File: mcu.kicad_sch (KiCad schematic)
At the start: 11 parts

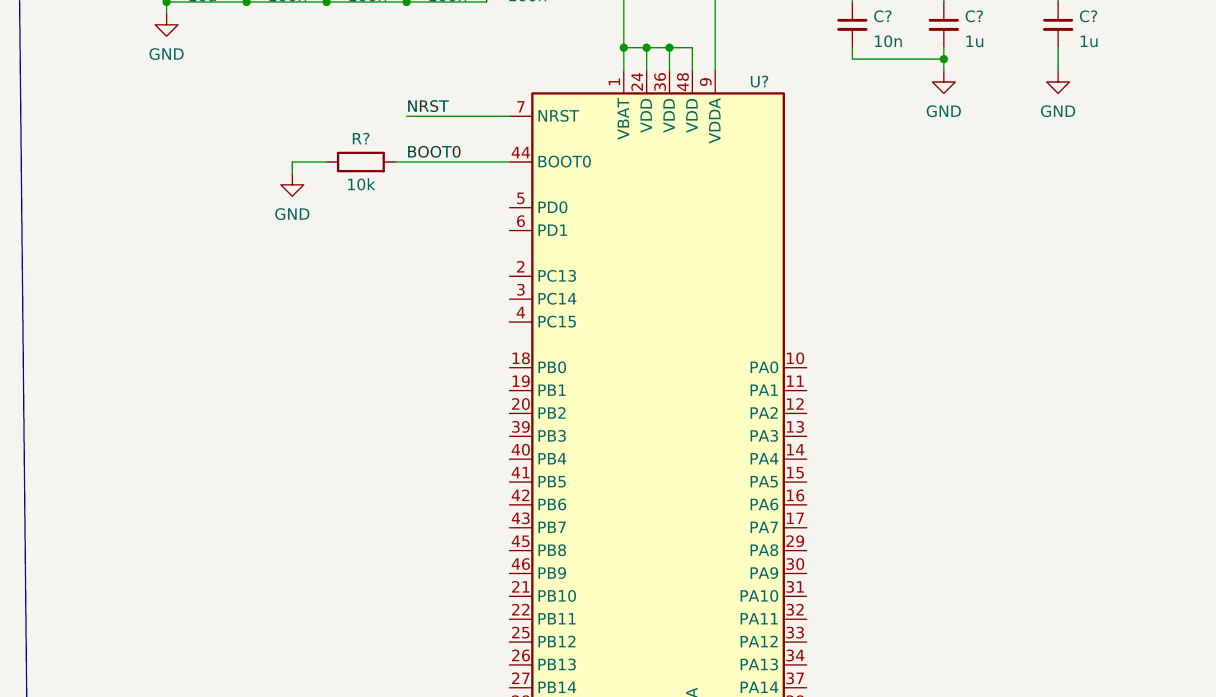
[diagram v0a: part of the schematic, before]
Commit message: Added crystal oscillator.
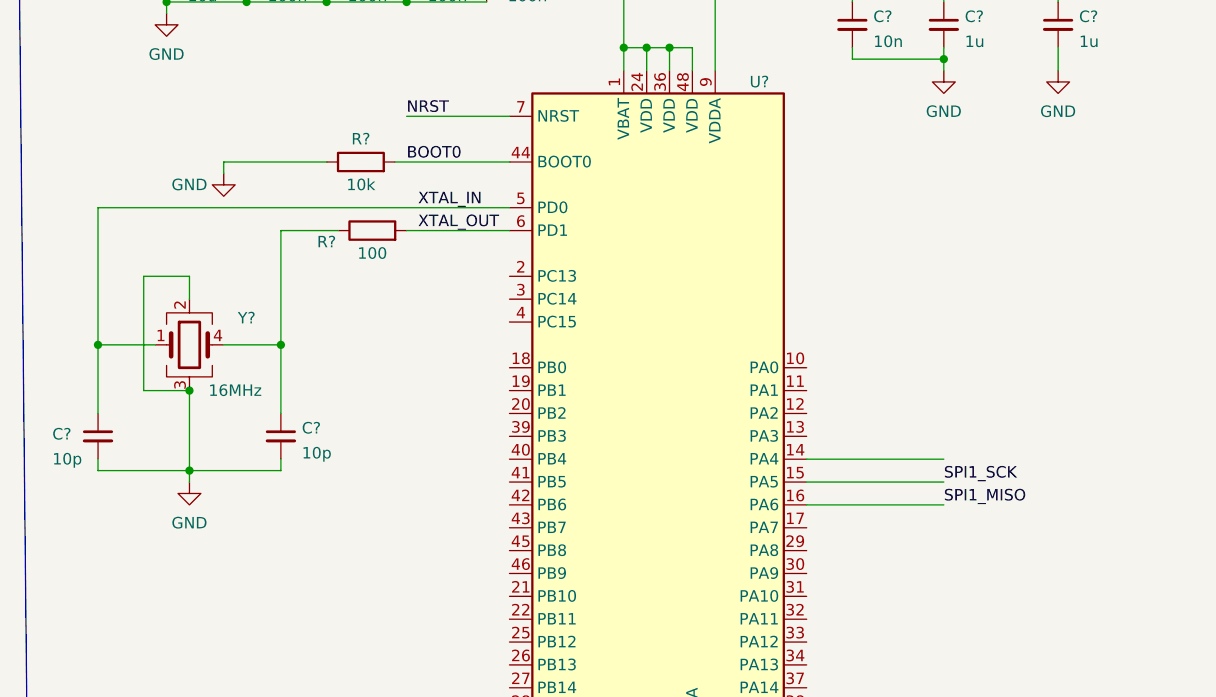
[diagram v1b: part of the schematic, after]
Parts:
- added C? (x2): 10p, symbol Device:C_Small
- added R?: 100, symbol Device:R
- added Y?: 16MHz, symbol Device:Crystal_GND23
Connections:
- net GND: now also C?.2, C?.2, Y?.2, Y?.3
- net SPI1_SCK: now reaches U?.15 (PA5)
- net SPI1_MISO: now reaches U?.16 (PA6)
- net XTAL_IN: now reaches U?.5 (PD0)
- net XTAL_IN: now also C?.1, Y?.1
- net XTAL_OUT: now reaches U?.6 (PD1)
- net XTAL_OUT: now also R?.2
- new net: C?.1, R?.1, Y?.4

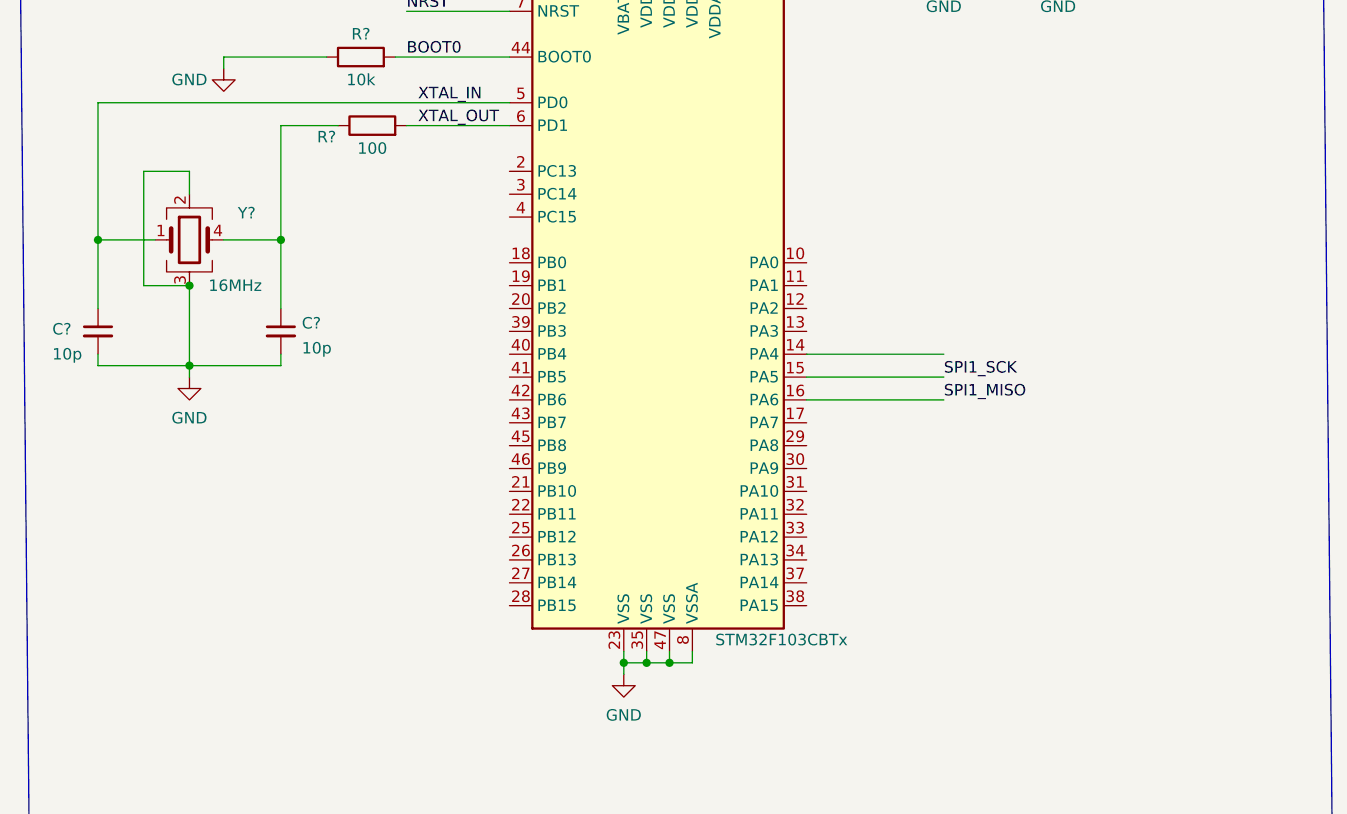
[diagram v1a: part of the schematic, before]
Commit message: Completed MCU circuitry
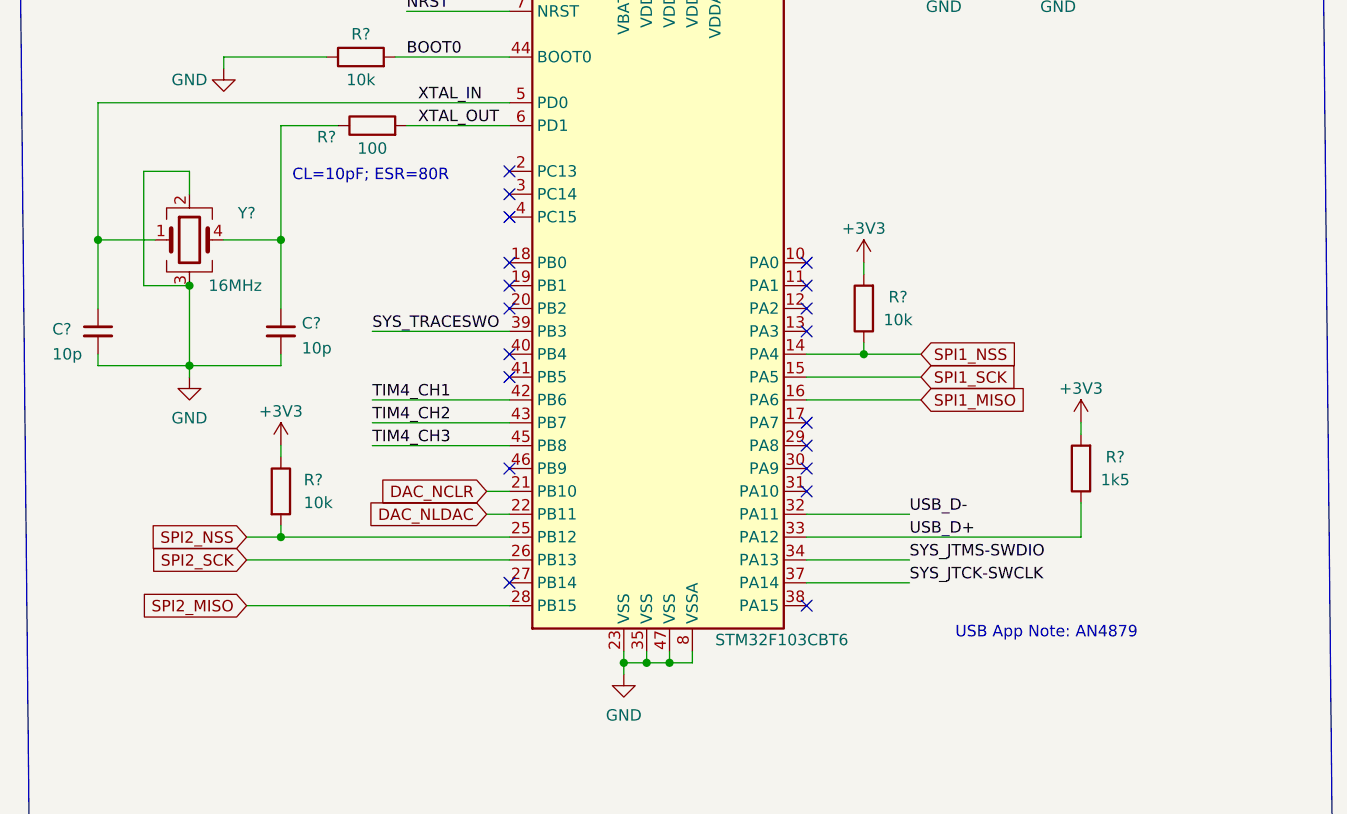
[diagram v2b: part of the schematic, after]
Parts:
- added R?: 1k5, symbol Device:R
- added R? (x2): 10k, symbol Device:R
- U?: value STM32F103CBTx -> STM32F103CBT6
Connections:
- net +3V3: now also R?.1, R?.2, R?.2
- net SPI1_NSS: now reaches U?.14 (PA4)
- net SPI1_NSS: now also R?.1
- net DAC_NCLR: now reaches U?.21 (PB10)
- net DAC_NLDAC: now reaches U?.22 (PB11)
- net SPI2_NSS: now reaches U?.25 (PB12)
- net SPI2_NSS: now also R?.2
- net SPI2_SCK: now reaches U?.26 (PB13)
- net SPI2_MISO: now reaches U?.28 (PB15)
- net USB_D-: now reaches U?.32 (PA11)
- net USB_D+: now reaches U?.33 (PA12)
- net USB_D+: now also R?.1
- net SYS_JTMS-SWDIO: now reaches U?.34 (PA13)
- net SYS_JTCK-SWCLK: now reaches U?.37 (PA14)
- net SYS_TRACESWO: now reaches U?.39 (PB3)
- net TIM4_CH1: now reaches U?.42 (PB6)
- net TIM4_CH2: now reaches U?.43 (PB7)
- net TIM4_CH3: now reaches U?.45 (PB8)
- no-connect marks 0 -> 19
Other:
- note added: "CL=10pF; ESR=80R"
- note added: "USB App Note: AN4879"

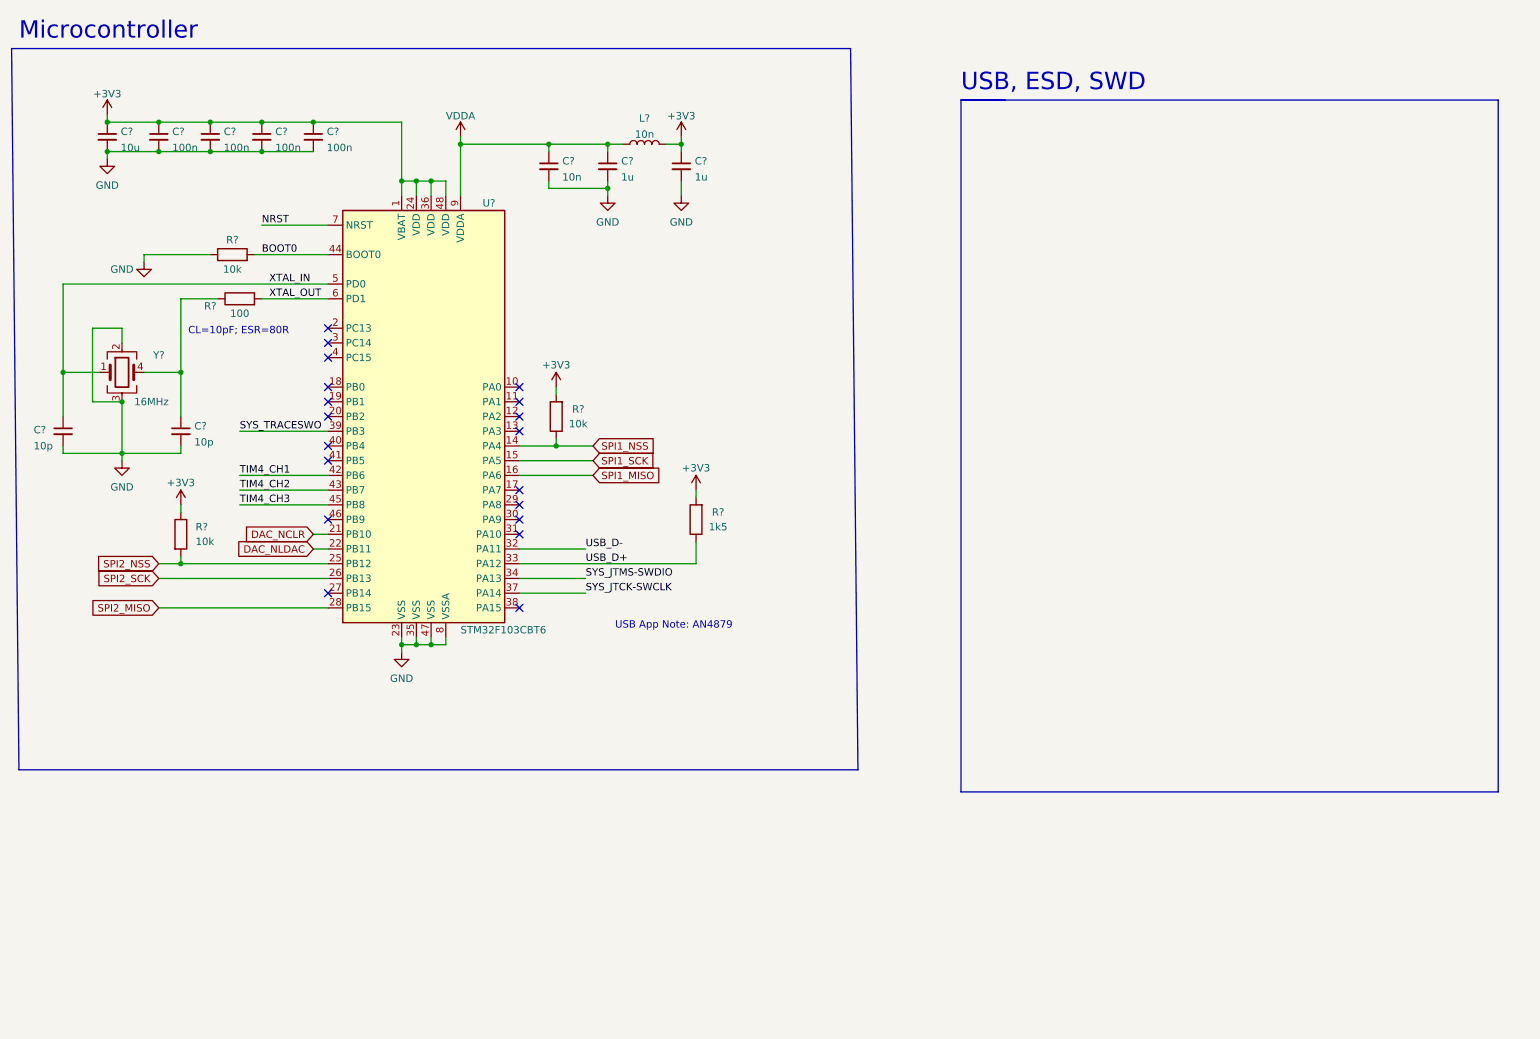
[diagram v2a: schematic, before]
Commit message: Completed USB Type C connection.
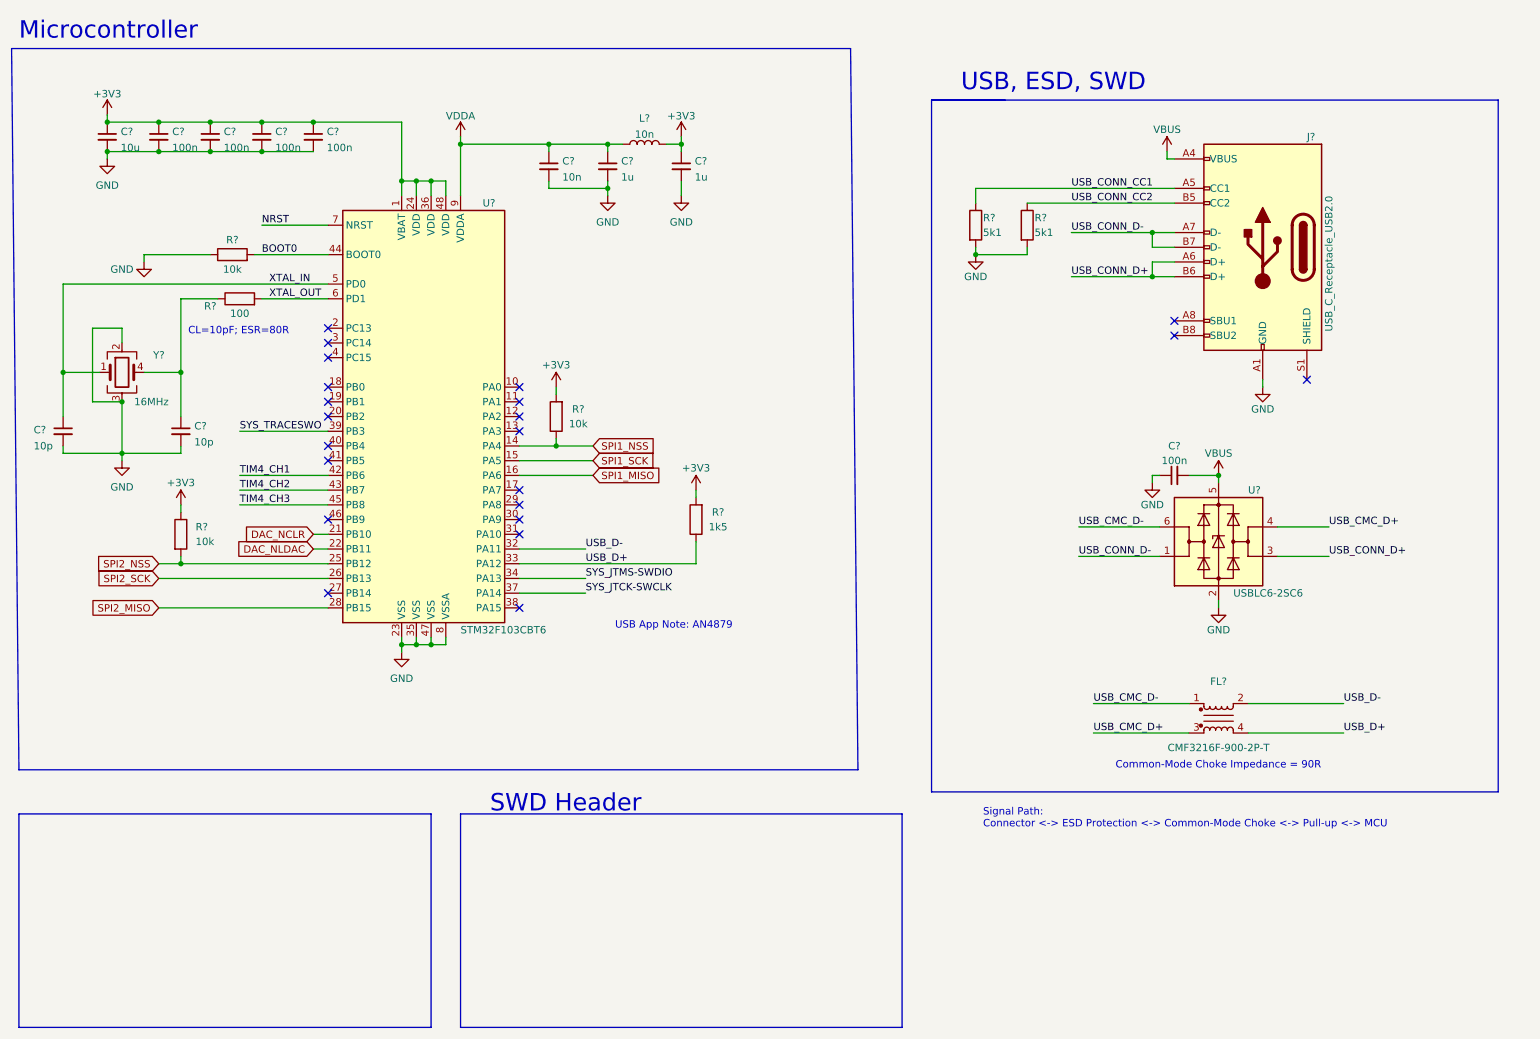
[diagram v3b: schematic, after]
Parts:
- added C?: 100n, symbol Device:C_Small
- added FL?: CMF3216F-900-2P-T, Inductor_THT:Choke_Schaffner_RN102-04-14.0x14.0mm, symbol Filter:Choke_Schaffner_RN102-0.3-02-12M
- added J?: USB_C_Receptacle_USB2.0, symbol Connector:USB_C_Receptacle_USB2.0
- added R? (x2): 5k1, symbol Device:R
- added U?: USBLC6-2SC6, Package_TO_SOT_SMD:SOT-23-6, symbol Power_Protection:USBLC6-2SC6
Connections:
- net GND: now also C?.1, J?.A1 (GND), J?.A12 (GND), J?.B1 (GND), J?.B12 (GND), R?.2, R?.2, U?.2 (GND)
- net USB_D+: now also FL?.4
- net USB_D-: now also FL?.2
- new net USB_CMC_D+: FL?.3, U?.4 (I/O2)
- new net USB_CMC_D-: FL?.1, U?.6 (I/O1)
- new net USB_CONN_CC1: J?.A5 (CC1), R?.1
- new net USB_CONN_CC2: J?.B5 (CC2), R?.1
- new net USB_CONN_D+: J?.A6 (D+), J?.B6 (D+), U?.3 (I/O2)
- new net USB_CONN_D-: J?.A7 (D-), J?.B7 (D-), U?.1 (I/O1)
- new net VBUS: C?.2, J?.A4 (VBUS), J?.A9 (VBUS), J?.B4 (VBUS), J?.B9 (VBUS), U?.5 (VBUS)
- no-connect marks 19 -> 22
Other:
- note added: "Common-Mode Choke Impedance = 90R"
- note added: "SWD Header"
- note added: "Signal Path: Connector <-> ESD Protection <-> Common-Mode Choke <-> Pull-up <-> MCU"
